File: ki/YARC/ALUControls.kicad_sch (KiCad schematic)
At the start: 10 parts, among them U107 74HC00, U123 74LS32, U124 74LS08, U125 74LS08, U126 74LS00, U127 74LS74, U129 74LS574, U130 74LS157, U131 74LS245, U93 74LS32

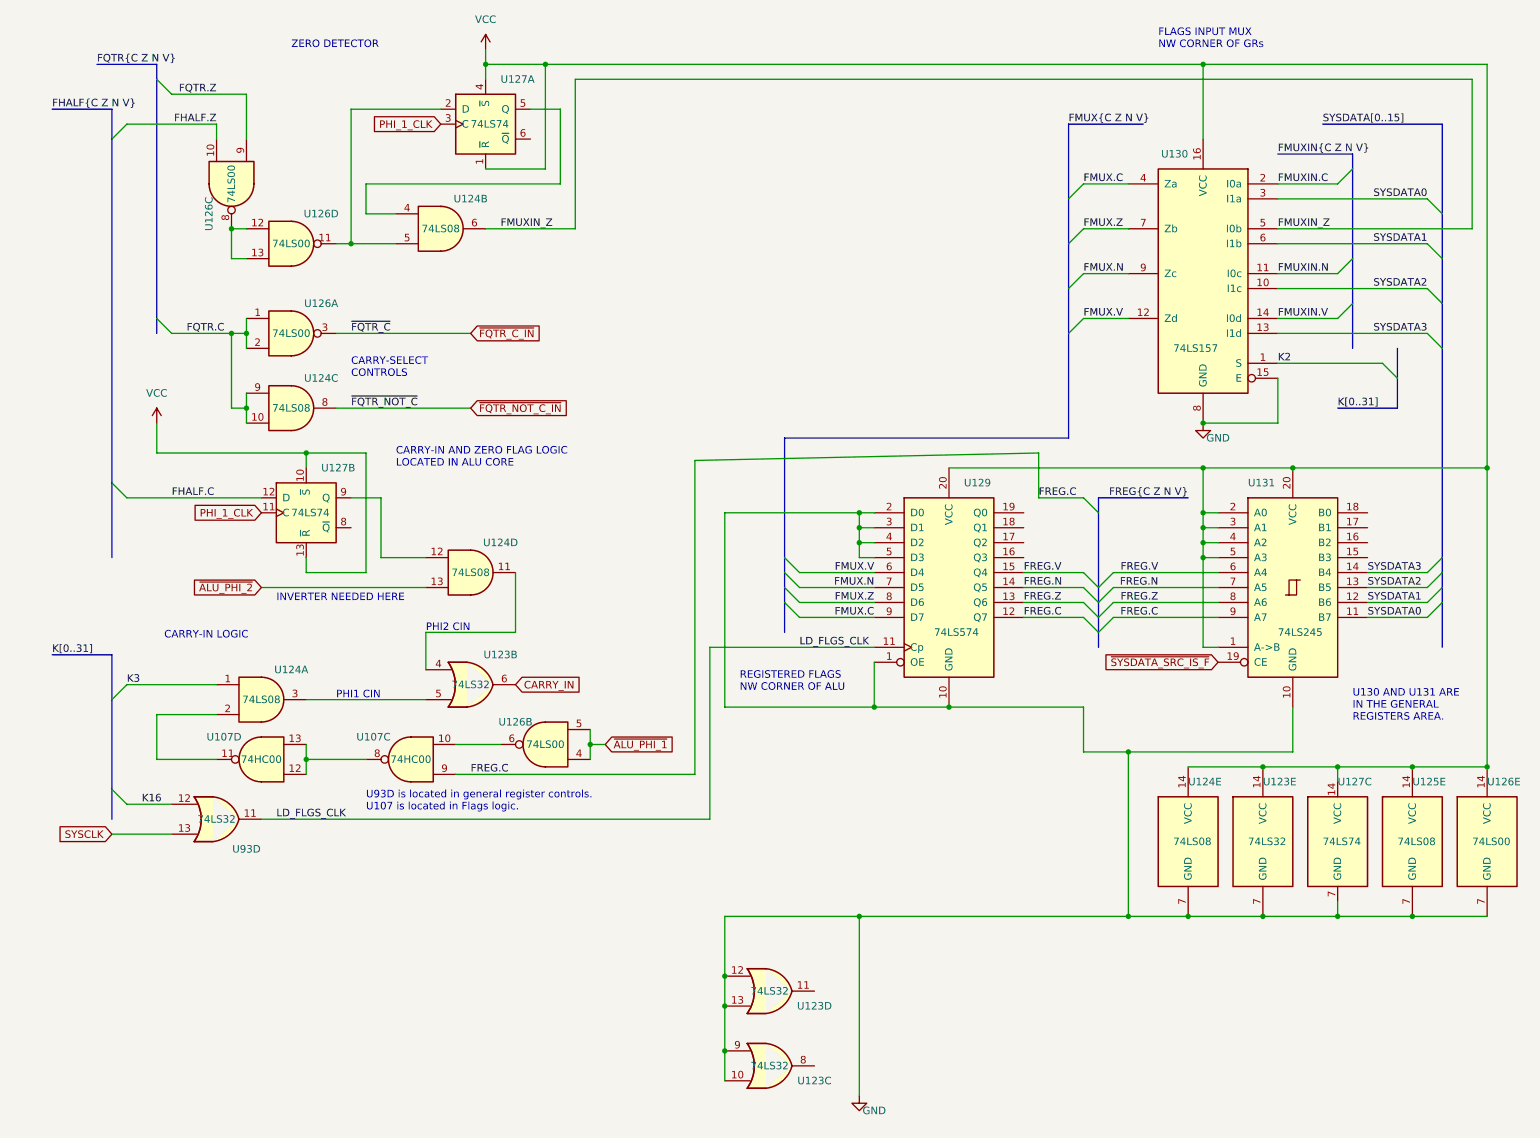
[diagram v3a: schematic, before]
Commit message: Start of final wiring. Relocate U135 and U136 close to clock distribution line in Flags circuit.
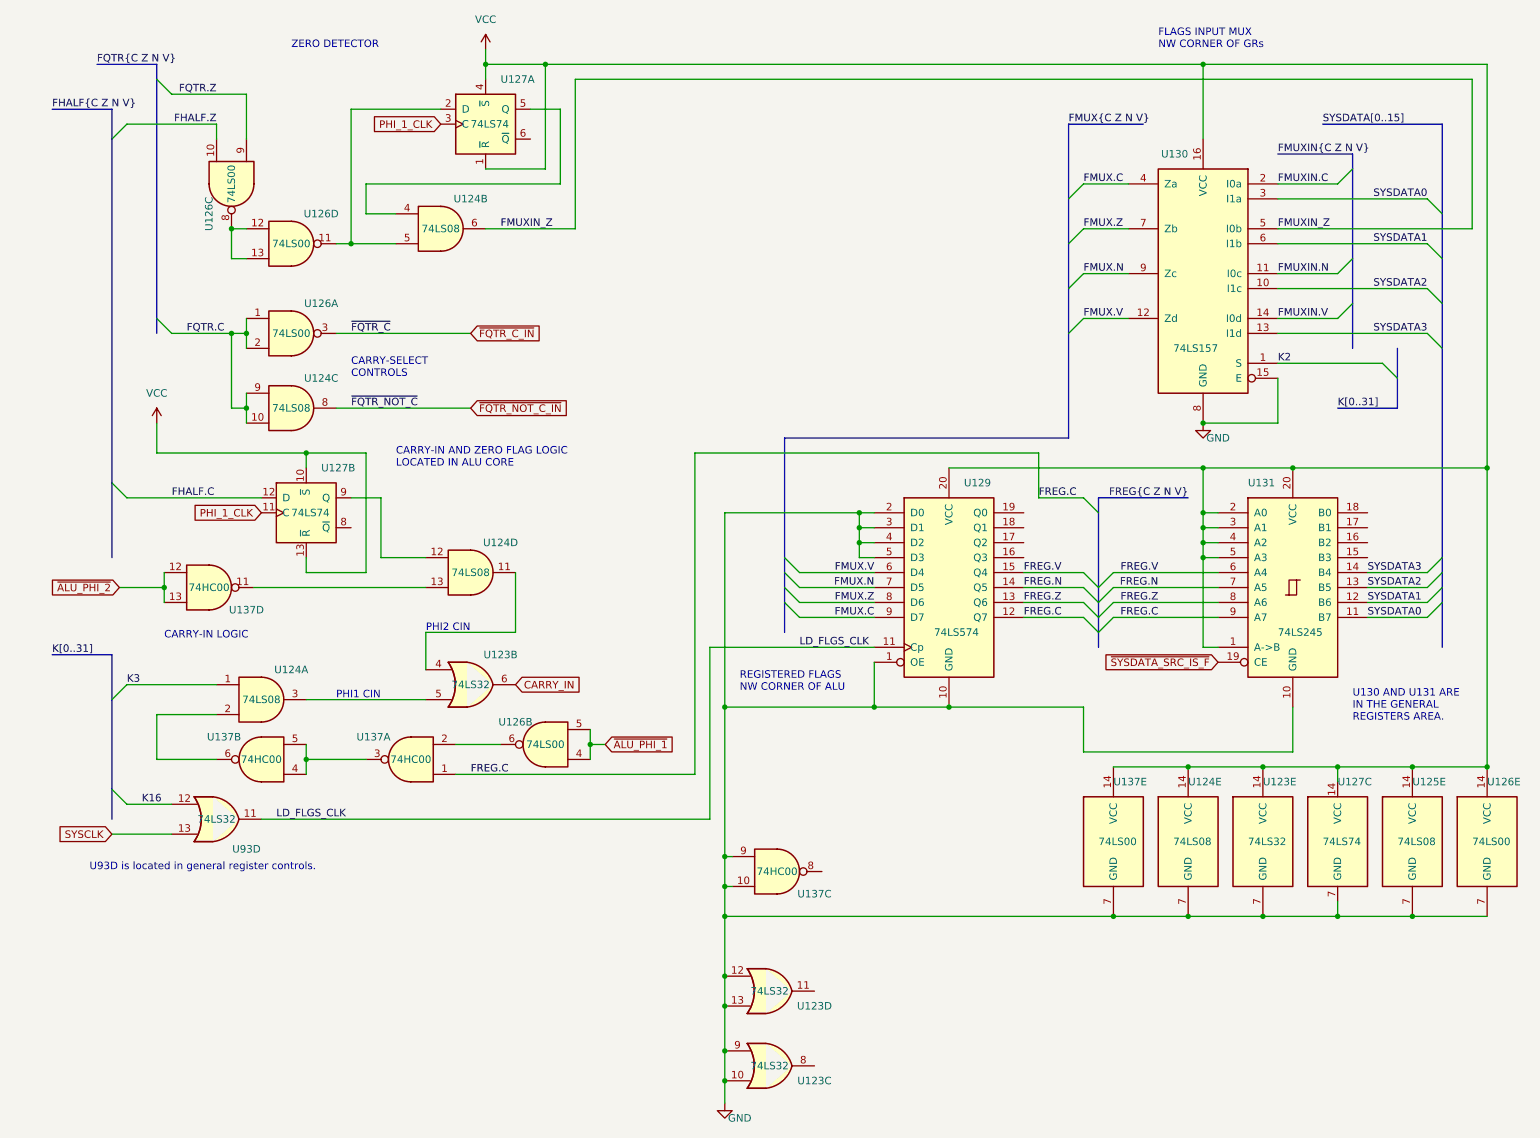
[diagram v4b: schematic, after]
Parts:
- added unit 5 of U137
- added unit 3 of U137
- added unit 4 of U137
- renumbered U107 to U137
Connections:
- net FREG.C: now also U137.1; no longer U137.9
- net GND: now also U137.10, U137.7 (GND), U137.9
- net VCC: now also U137.14 (VCC)
- net ~{ALU_PHI_2}: now also U137.12, U137.13; no longer U124.13
- net at U126.6: now also U137.2; no longer U137.10
- net at U124.2: now also U137.6; no longer U137.11
- new net: U137.3, U137.4, U137.5
- new net: U124.13, U137.11
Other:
- note added: "U93D is located in general register controls."
- note removed: "INVERTER NEEDED HERE"
- note removed: "U93D is located in general register controls. U107 is located in Flags logic."

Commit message: Ongoing corrections and improvements. No major additions.
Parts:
- removed unit 5 of U126
- removed unit 2 of U126
- removed unit 4 of U126
- removed unit 3 of U126
- removed unit 3 of U137
- added U126: 74LS08, symbol 74xx:74LS08
- renumbered U126 to U137
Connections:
- net FHALF.Z: now also U126.2
- net FQTR.C: now also U137.10, U137.9; no longer U137.1, U137.2
- net FQTR.Z: now also U126.1
- net FREG.C: now also U126.5; no longer U137.1
- net GND: now also U137.4, U137.5, U126.10, U126.12, U126.13, U126.7 (GND), U126.9
- net VCC: now also U126.14 (VCC)
- net ~{ALU_PHI_1}: now also U137.1, U137.2
- net ~{FQTR_C_IN}: now also U137.8; no longer U137.3
- net at U124.5, U127.2 (D): now also U126.3
- net at U124.2: now also U126.6; no longer U137.6
- new net: U126.4, U137.3
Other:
- moved on the sheet: U124B

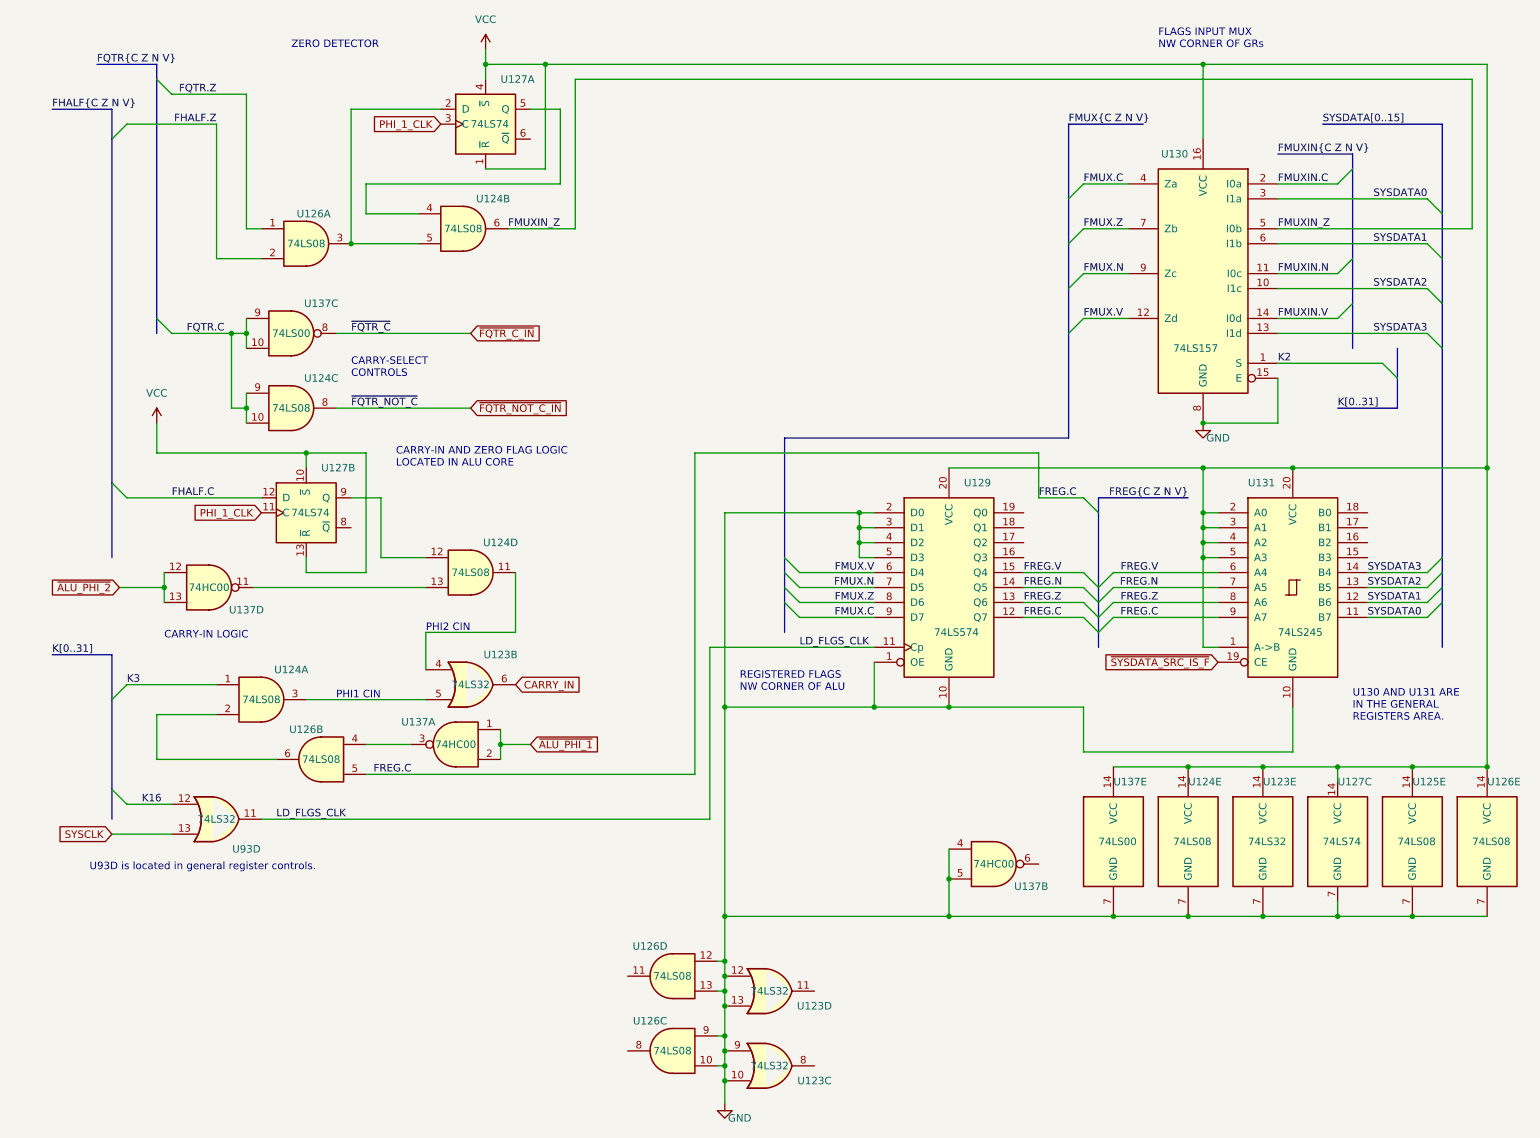
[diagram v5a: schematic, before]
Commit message: Wiring of entire YARC is complete
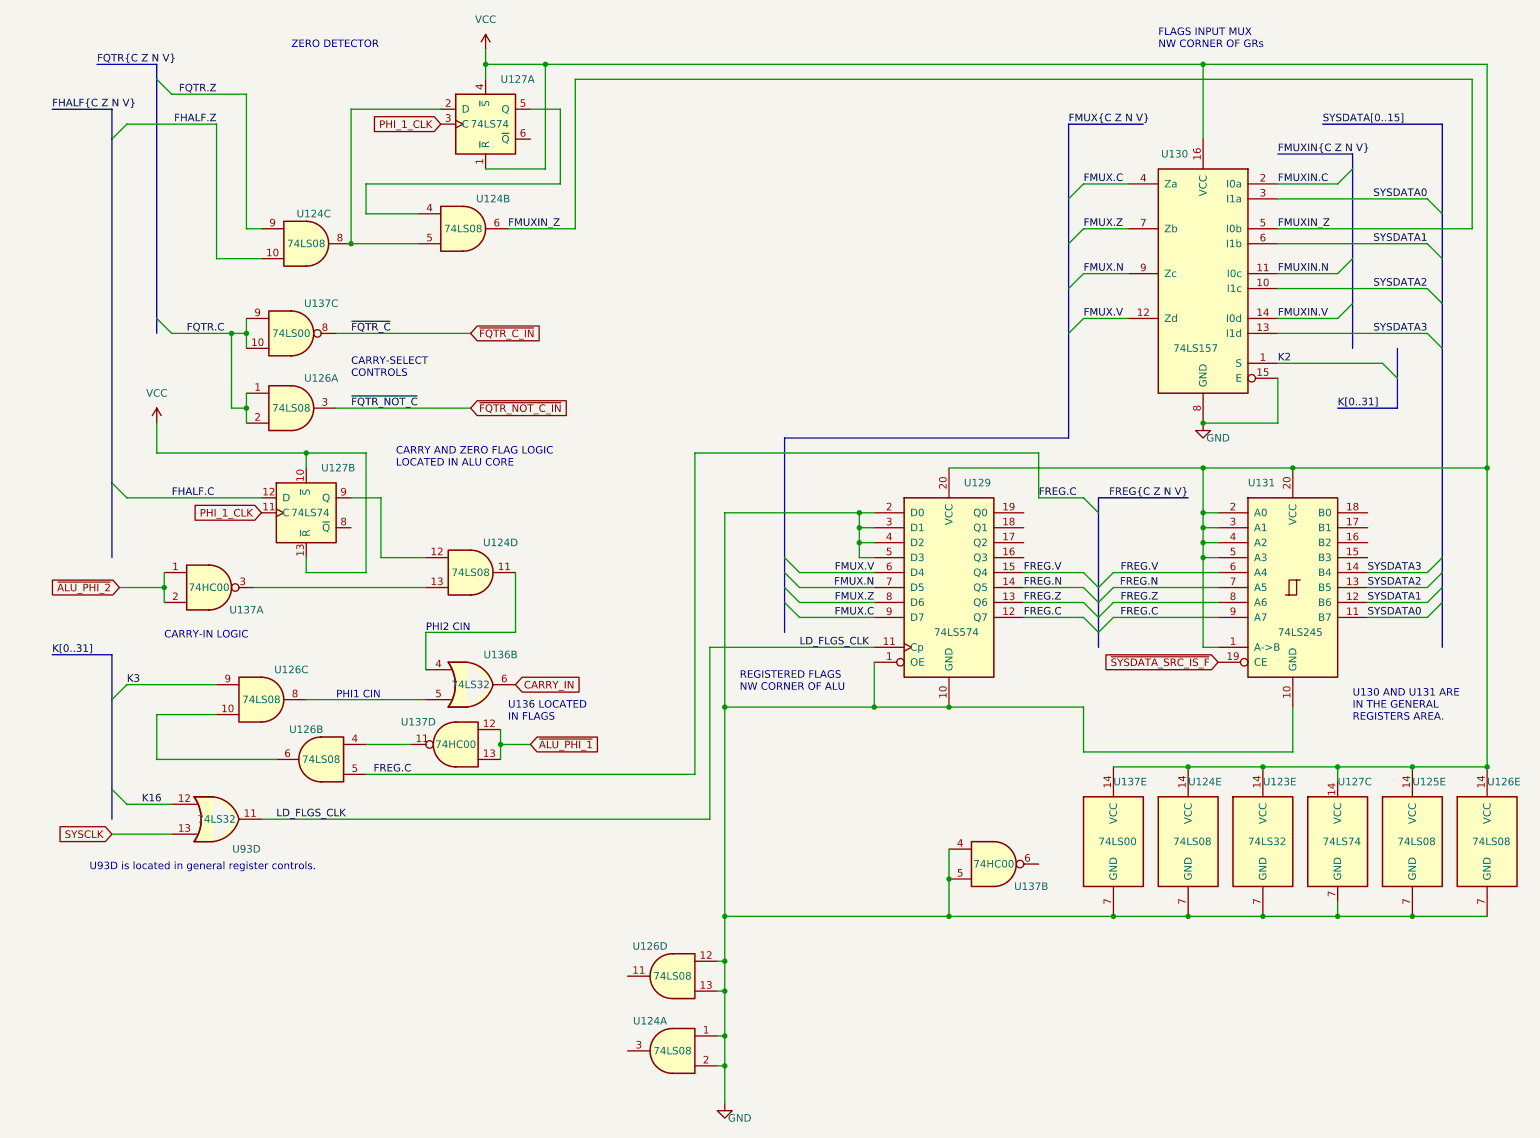
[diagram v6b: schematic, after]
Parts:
- removed unit 4 of U123
- removed unit 3 of U123
- renumbered U126 to U124, U124 to U126, U123 to U136
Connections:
- net FHALF.Z: now also U124.10; no longer U124.2
- net FQTR.C: now also U126.1, U126.2; no longer U126.10, U126.9
- net FQTR.Z: now also U124.9; no longer U124.1
- net GND: now also U124.1, U124.2; no longer U124.10, U124.9
- net K3: now also U126.9; no longer U126.1
- net ~{ALU_PHI_1}: now also U137.12, U137.13; no longer U137.1, U137.2
- net ~{ALU_PHI_2}: now also U137.1, U137.2; no longer U137.12, U137.13
- net ~{FQTR_NOT_C_IN}: now also U126.3; no longer U126.8
- net at U126.4: now also U137.11; no longer U137.3
- net at U124.5, U127.2 (D): now also U124.8; no longer U124.3
- net at U126.6: now also U126.10; no longer U126.2
- net at U136.5: now also U126.8; no longer U126.3
- net at U124.13: now also U137.3; no longer U137.11
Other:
- note added: "CARRY AND ZERO FLAG LOGIC LOCATED IN ALU CORE"
- note added: "U136 LOCATED IN FLAGS"
- note removed: "CARRY-IN AND ZERO FLAG LOGIC LOCATED IN ALU CORE"

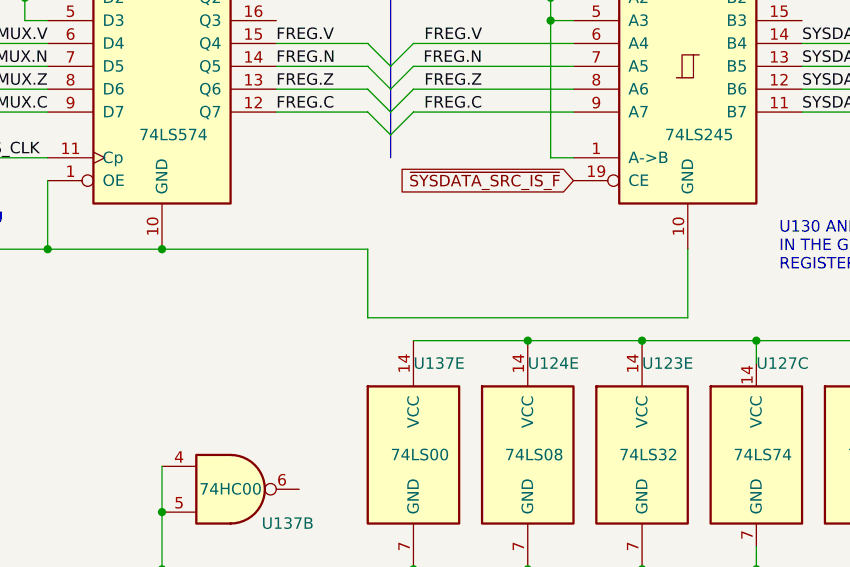
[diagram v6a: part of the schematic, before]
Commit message: Add delay line for general register write signal. Minor corrections and cleanups.
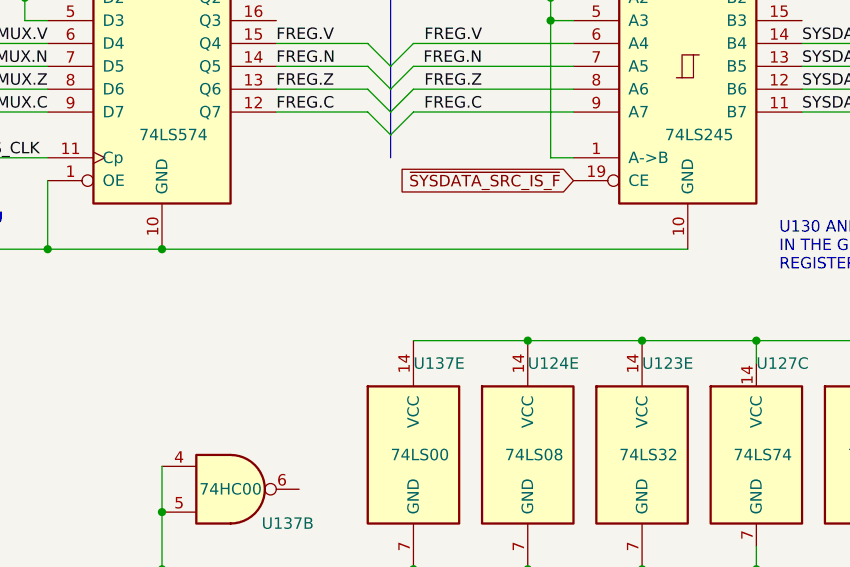
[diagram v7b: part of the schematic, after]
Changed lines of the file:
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@@
-    (stroke (width 0) (type default) (color 0 0 0 0))
-  )
-  (wire (pts (xy 190.5 139.7) (xy 226.06 139.7))
     (stroke (width 0) (type default) (color 0 0 0 0))
   )
@@
     (stroke (width 0) (type default) (color 0 0 0 0))
   )
-  (wire (pts (xy 190.5 132.08) (xy 190.5 139.7))
-    (stroke (width 0) (type default) (color 0 0 0 0))
-  )
   (wire (pts (xy 96.52 138.43) (xy 91.44 138.43))
     (stroke (width 0) (type default) (color 0 0 0 0))
@@
     (stroke (width 0) (type default) (color 0 0 0 0))
   )
-  (wire (pts (xy 226.06 132.08) (xy 226.06 139.7))
-    (stroke (width 0) (type default) (color 0 0 0 0))
-  )
   (bus (pts (xy 193.04 114.3) (xy 193.04 116.84))
     (stroke (width 0) (type default) (color 0 0 0 0))
   )
-  (wire (pts (xy 190.5 132.08) (xy 167.64 132.08))
-    (stroke (width 0) (type default) (color 0 0 0 0))
-  )
+  (wire (pts (xy 167.64 132.08) (xy 226.06 132.08))
+    (stroke (width 0) (type default) (color 0 0 0 0))
+  )
